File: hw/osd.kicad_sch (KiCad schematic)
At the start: 62 parts, among them U801 SN74CBTLV3125RGYR, U802 XLV320ADC5140IRTWR, U803 SN74CBTLV3125RGYR, U804 SN74CBTLV3125RGYR, U805 SN74CBTLV3125RGYR

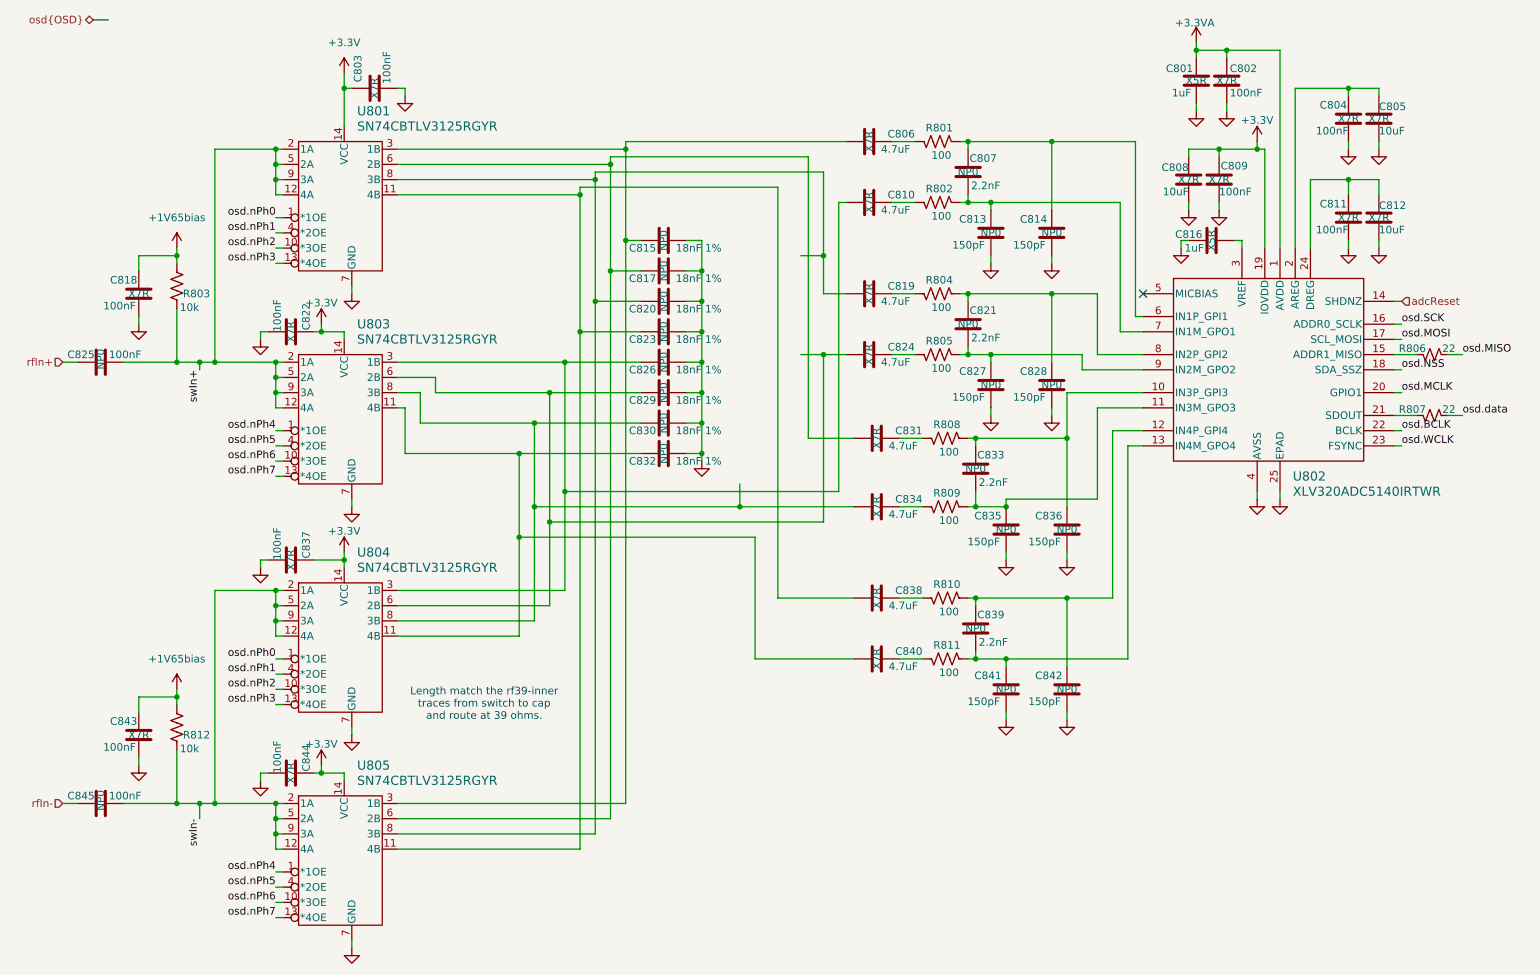
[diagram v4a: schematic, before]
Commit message: Not proud of the rats nest of controls for attenuator and filter, but now I have four filters (not five), all DRC pass, 3D renders properly, and I may tidy it up a bit later.
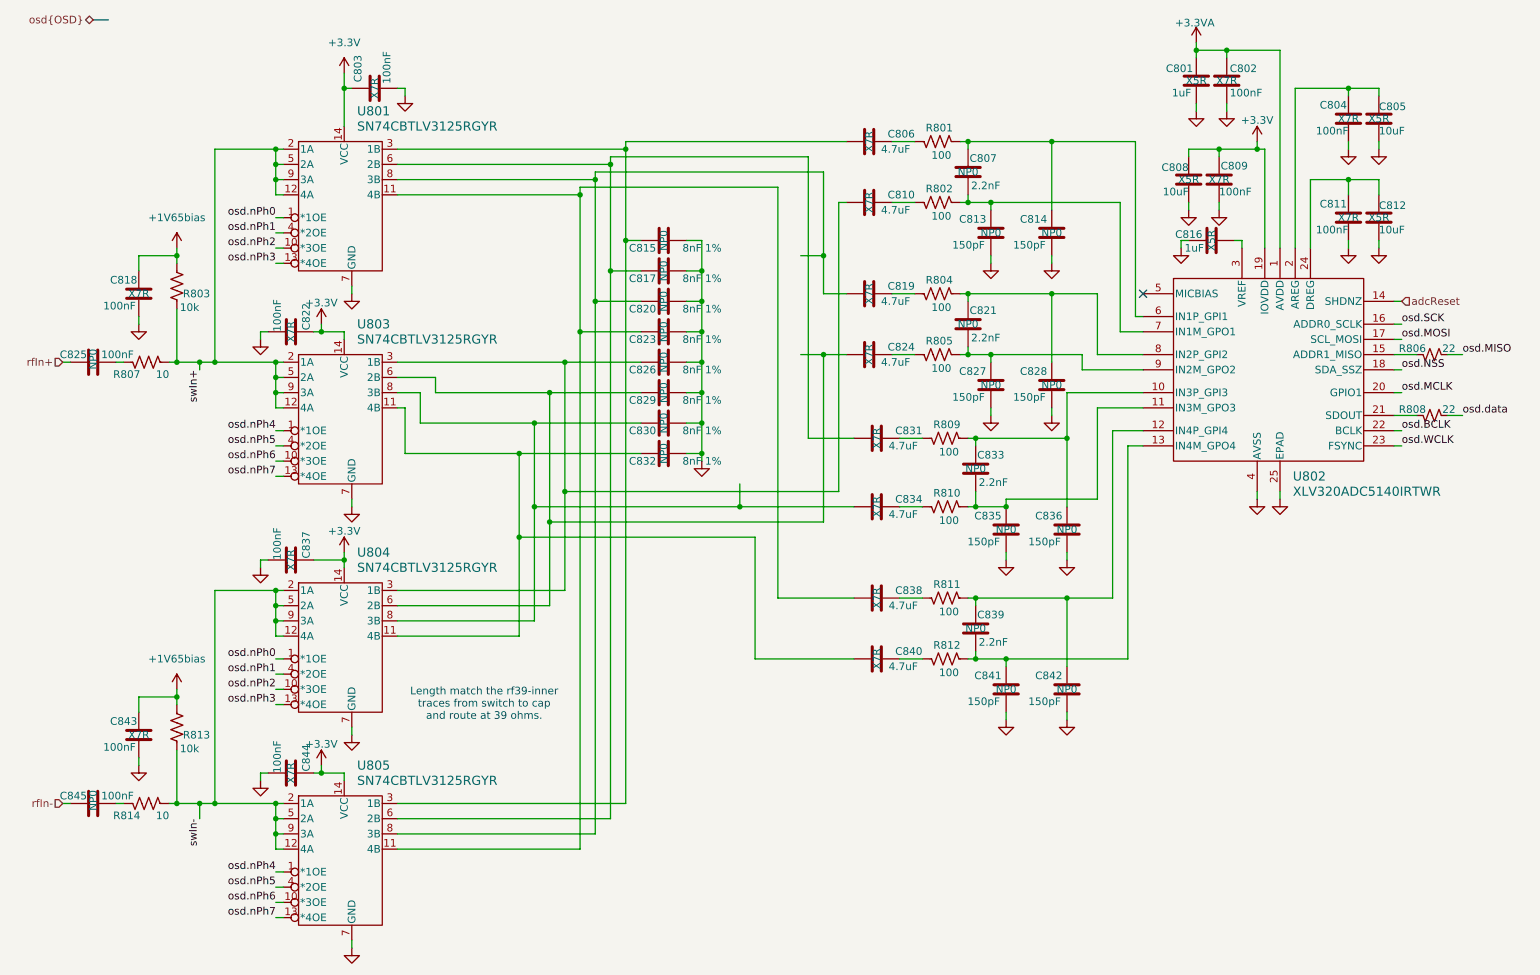
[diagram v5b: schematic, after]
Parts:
- added R807, R814: 10, Resistor_SMD:R_0402_1005Metric, symbol Device:R_US
- C805, C808, C812: footprint Capacitor_SMD:C_0603_1608Metric -> Capacitor_SMD:C_0402_1005Metric; cap-type X7R -> X5R; working-voltage 25V -> 10V
- C807, C821, C833, C839: footprint Capacitor_SMD:C_0603_1608Metric -> Capacitor_SMD:C_0402_1005Metric
- C815, C817, C820, C823, C826, C829, C830, C832: value 18nF 1% -> 8nF 1%
- renumbered R807 to R808, R808 to R809, R809 to R810, R810 to R811, R811 to R812, R812 to R813
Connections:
- net swIn+: now also R807.2; no longer C825.2
- net swIn-: now also R814.2; no longer C845.2
- new net: C845.2, R814.1
- new net: C825.2, R807.1
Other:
- moved on the sheet: C825, C845

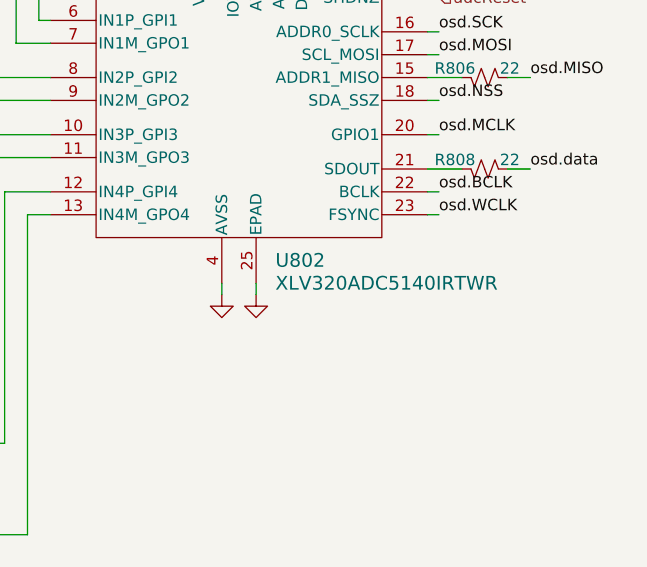
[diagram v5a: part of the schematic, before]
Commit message: Set up for DVT2 PCBA build at JLCPCB
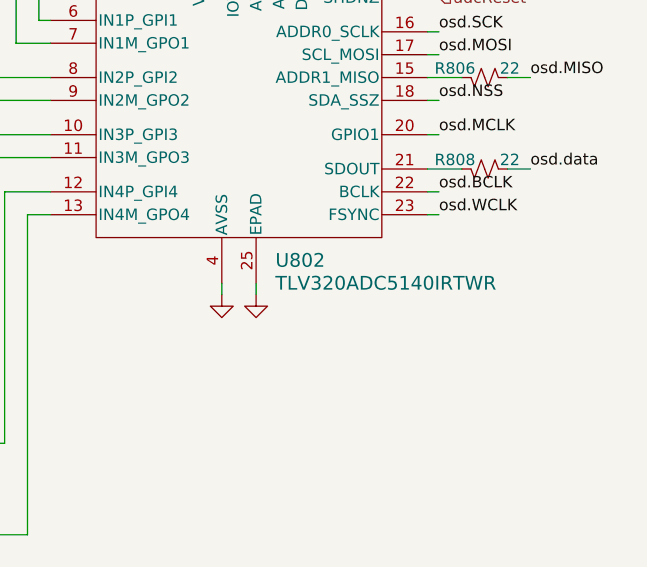
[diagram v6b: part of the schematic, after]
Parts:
- C801, C816: MPN GRM155R61E105KE11D -> (none)
- C802, C803, C804, C809, C811, C818, C822, C837, C843, C844: MPN C0805F104K1RACAUTO -> (none)
- C805, C808, C812: MPN TAJD106K050RNJ -> (none)
- C813, C814, C827, C828, C835, C836, C841, C842: MPN 06033A151FAT2A -> (none)
- C815, C817, C820, C823, C826, C829, C830, C832: JLCPCBpn C106211 -> (none)
- C825, C845: Mouser Part Number (none) -> 81-GRM3195C2A104JA1D
- U802: value XLV320ADC5140IRTWR -> TLV320ADC5140IRTWR; MFG (none) -> TI; MPN (none) -> TLV320ADC5140IRTWR
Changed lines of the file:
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@@
 			)
 		)
+		(property "Mouser Part Number" "81-GRM3195C2A104JA1D"
+			(at 25.4 148.59 90)
+			(effects
+				(font
+					(size 1.27 1.27)
+				)
+				(hide yes)
+			)
+		)
 		(pin "2"
 		)
@@
 			)
 		)
-		(property "MPN" "TAJD106K050RNJ"
+		(property "MPN" ""
 			(at 486.41 -107.95 0)
 			(effects
@@
 			)
 		)
-		(property "JLCPCBpn" "C106211"
+		(property "JLCPCBpn" ""
 			(at 120.65 64.77 0)
 			(effects
@@
 			)
 		)
-		(property "MPN" "C0805F104K1RACAUTO"
+		(property "MPN" ""
 			(at 414.02 -109.22 0)
 			(effects
@@
 			)
 		)
-		(property "Value" "XLV320ADC5140IRTWR"
+		(property "Value" "TLV320ADC5140IRTWR"
 			(at 225.6633 96.52 0)
 			(effects
@@
 			)
 		)
-		(property "Datasheet" "XLV320ADC5140IRTWR"
+		(property "Datasheet" "https://www.ti.com/lit/gpn/tlv320adc5140"
 			(at 142.24 132.08 0)
 			(effects
@@
 			)
 		)
+		(property "cap-type" ""
+			(at 220.98 74.93 0)
+			(effects
+				(font
+					(size 1.27 1.27)
+				)
+			)
+		)
+		(property "r-power" ""
+			(at 220.98 74.93 0)
+			(effects
+				(font
+					(size 1.27 1.27)
+				)
+			)
+		)
+		(property "label" ""
+			(at 220.98 74.93 0)
+			(effects
+				(font
+					(size 1.27 1.27)
+				)
+			)
+		)
+		(property "MPN" "TLV320ADC5140IRTWR"
+			(at 220.98 74.93 0)
+			(effects
+				(font
+					(size 1.27 1.27)
+				)
+				(hide yes)
+			)
+		)
+		(property "MFG" "TI"
+			(at 220.98 74.93 0)
+			(effects
+				(font
+					(size 1.27 1.27)
+				)
+				(hide yes)
+			)
+		)
 		(pin "2"
 		)
@@
 			)
 		)
-		(property "JLCPCBpn" "C106211"
+		(property "JLCPCBpn" ""
 			(at 120.65 80.01 0)
 			(effects
@@
 			)
 		)
-		(property "JLCPCBpn" "C106211"
+		(property "JLCPCBpn" ""
 			(at 120.65 74.93 0)
 			(effects
@@
 			)
 		)
-		(property "MPN" "GRM155R61E105KE11D"
+		(property "MPN" ""
 			(at 88.9 -182.88 0)
 			(effects
@@
 			)
 		)
-		(property "MPN" "06033A151FAT2A"
+		(property "MPN" ""
 			(at 17.78 53.34 0)
 			(effects
@@
 			)
 		)
-		(property "MPN" "C0805F104K1RACAUTO"
+		(property "MPN" ""
 			(at 317.5 -20.32 0)
 			(effects
@@
 			)
 		)
-		(property "MPN" "06033A151FAT2A"
+		(property "MPN" ""
 			(at 25.4 2.54 0)
 			(effects
@@
 			)
 		)
-		(property "MPN" "C0805F104K1RACAUTO"
+		(property "MPN" ""
 			(at 130.81 -26.67 0)
 			(effects
@@
 			)
 		)
-		(property "MPN" "06033A151FAT2A"
+		(property "MPN" ""
 			(at 15.24 2.54 0)
 			(effects
@@
 			)
 		)
-		(property "MPN" "TAJD106K050RNJ"
+		(property "MPN" ""
 			(at 486.41 -124.46 0)
 			(effects
@@
 			)
 		)
-		(property "MPN" "C0805F104K1RACAUTO"
+		(property "MPN" ""
 			(at 181.61 314.96 0)
 			(effects
@@
 			)
 		)
-		(property "JLCPCBpn" "C106211"
+		(property "JLCPCBpn" ""
 			(at 120.65 69.85 0)
 			(effects
@@
 			)
 		)
-		(property "MPN" "06033A151FAT2A"
+		(property "MPN" ""
 			(at 27.94 53.34 0)
 			(effects
@@
 			)
 		)
-		(property "MPN" "06033A151FAT2A"
+		(property "MPN" ""
 			(at 17.78 26.67 0)
 			(effects
@@
 			)
 		)
-		(property "JLCPCBpn" "C106211"
+		(property "JLCPCBpn" ""
 			(at 120.65 54.61 0)
 			(effects
@@
 			)
 		)
-		(property "MPN" "TAJD106K050RNJ"
+		(property "MPN" ""
 			(at -38.1 -114.3 0)
 			(effects
@@
 			)
 		)
-		(property "MPN" "06033A151FAT2A"
+		(property "MPN" ""
 			(at 27.94 26.67 0)
 			(effects
@@
 			)
 		)
-		(property "JLCPCBpn" "C106211"
+		(property "JLCPCBpn" ""
 			(at 120.65 59.69 0)
 			(effects
@@
 			)
 		)
-		(property "MPN" "C0805F104K1RACAUTO"
+		(property "MPN" ""
 			(at 115.57 66.04 0)
 			(effects
@@
 			)
 		)
-		(property "MPN" "C0805F104K1RACAUTO"
+		(property "MPN" ""
 			(at 317.5 -36.83 0)
 			(effects
@@
 			)
 		)
-		(property "MPN" "C0805F104K1RACAUTO"
+		(property "MPN" ""
 			(at 181.61 353.06 0)
 			(effects
@@
 			)
 		)
-		(property "MPN" "C0805F104K1RACAUTO"
+		(property "MPN" ""
 			(at -50.8 274.32 0)
 			(effects
@@
 			)
 		)
-		(property "JLCPCBpn" "C106211"
+		(property "JLCPCBpn" ""
 			(at 120.65 90.17 0)
 			(effects
@@
 			)
 		)
-		(property "MPN" "06033A151FAT2A"
+		(property "MPN" ""
 			(at 25.4 -22.86 0)
 			(effects
@@
 			)
 		)
+		(property "Mouser Part Number" "81-GRM3195C2A104JA1D"
+			(at 25.4 74.93 90)
+			(effects
+				(font
+					(size 1.27 1.27)
+				)
+				(hide yes)
+			)
+		)
 		(pin "2"
 		)
@@
 			)
 		)
-		(property "MPN" "06033A151FAT2A"
+		(property "MPN" ""
 			(at 15.24 -22.86 0)
 			(effects
@@
 			)
 		)
-		(property "JLCPCBpn" "C106211"
+		(property "JLCPCBpn" ""
 			(at 120.65 85.09 0)
 			(effects
@@
 			)
 		)
-		(property "MPN" "C0805F104K1RACAUTO"
+		(property "MPN" ""
 			(at 115.57 -7.62 0)
 			(effects
@@
 			)
 		)
-		(property "MPN" "C0805F104K1RACAUTO"
+		(property "MPN" ""
 			(at 181.61 388.62 0)
 			(effects
@@
 			)
 		)
-		(property "MPN" "GRM155R61E105KE11D"
+		(property "MPN" ""
 			(at 447.04 151.13 0)
 			(effects

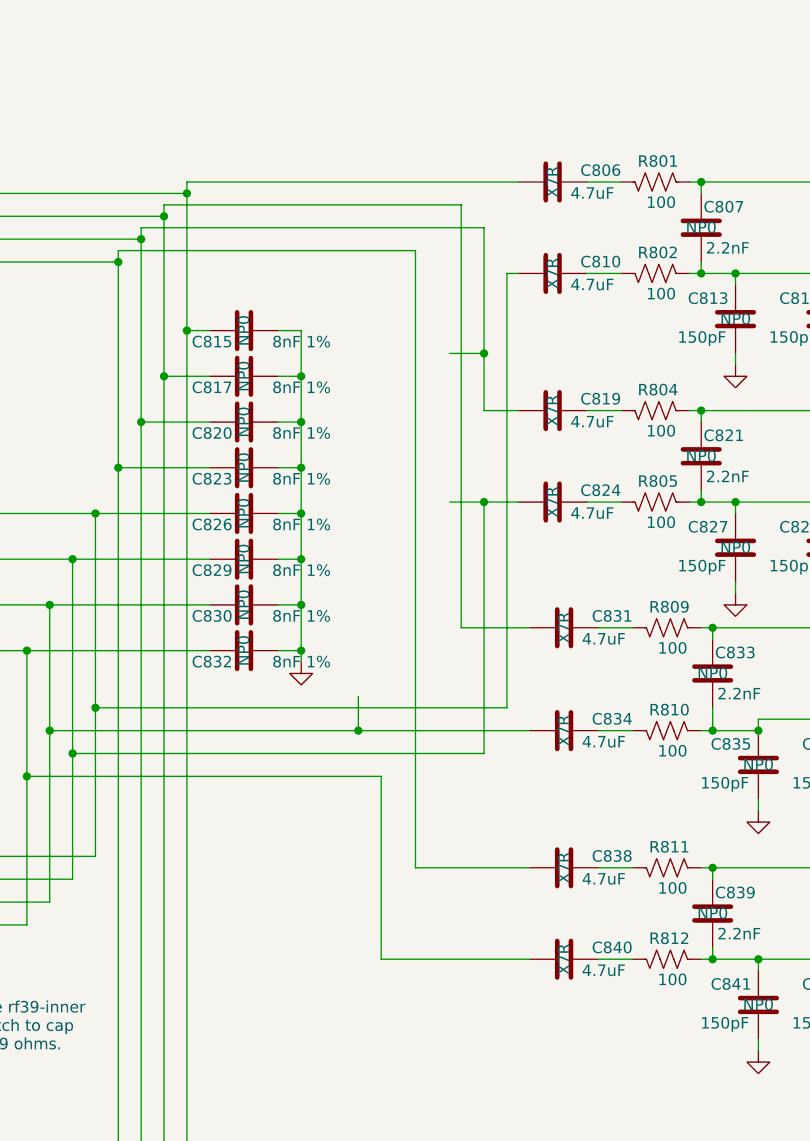
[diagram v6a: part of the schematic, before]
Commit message: Switch to parts I can source from Mouser
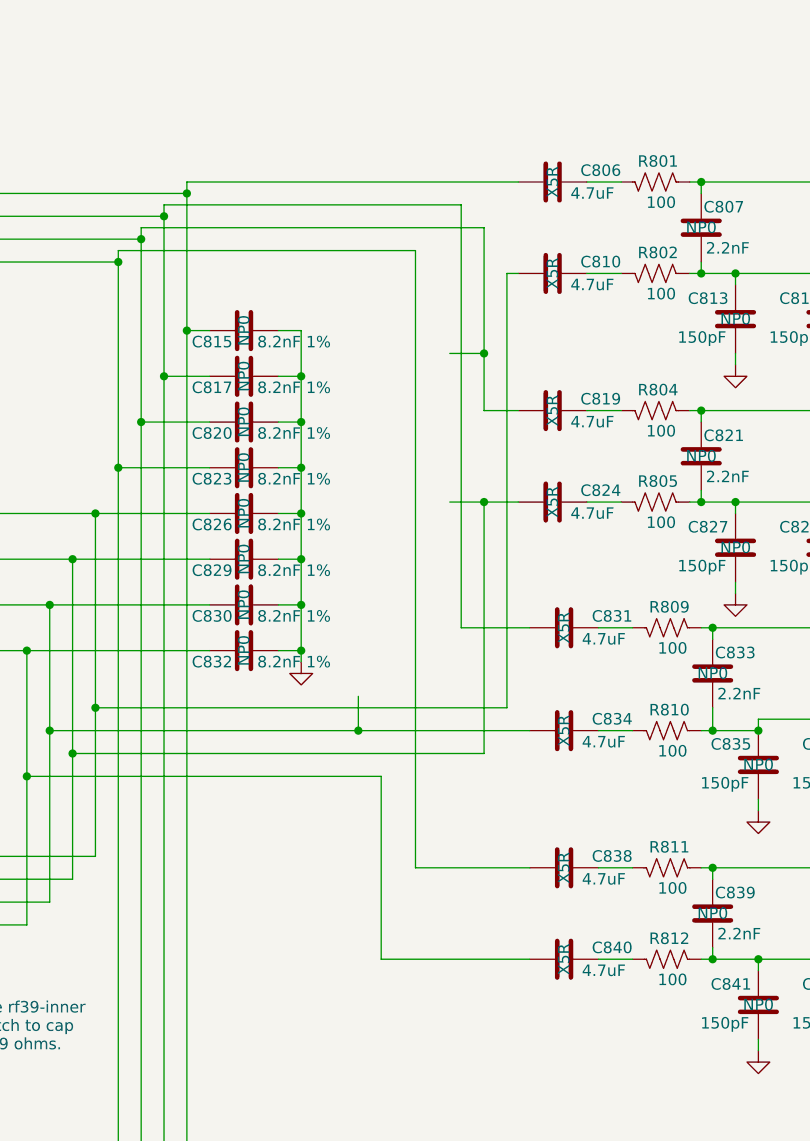
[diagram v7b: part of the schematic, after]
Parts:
- C801, C816: MFG (none) -> muRata; MPN (none) -> GRM155R61E105MA12D; Mouser Part Number (none) -> 81-GRM155R61E105MA2D
- C802, C803, C804, C809, C811, C818, C822, C837, C843, C844: MFG (none) -> muRata; MPN (none) -> GCM155R71H104KE02D; Mouser Part Number (none) -> 81-GCM155R71H104KE2D
- C805, C808, C812: MFG (none) -> Samsung; MPN (none) -> CL05A106MP6NUN8; Mouser Part Number (none) -> 187-CL05A106MP6NUN8
- C806, C810, C819, C824, C831, C834, C838, C840: MFG (none) -> Kyocera; MPN (none) -> CM05X5R475M10AH; Mouser Part Number (none) -> 346-CM05X5R475M10AH; cap-type X7R -> X5R; working-voltage 25V -> 10V
- C807, C821, C833, C839: MFG (none) -> KEMET; MPN (none) -> C0402C222K3GECTU; Mouser Part Number (none) -> 80-C0402C222K3GECTU
- C813, C814, C827, C828, C835, C836, C841, C842: MFG (none) -> Kyocera; MPN (none) -> 04023A151JAT2A; Mouser Part Number (none) -> 581-04023A151J
- C815, C817, C820, C823, C826, C829, C830, C832: value 8nF 1% -> 8.2nF 1%; MFG (none) -> Kyocera; MPN (none) -> 08053A822FAT2A; Mouser Part Number (none) -> 581-08053A822FAT2A
- C825, C845: MFG (none) -> muRata

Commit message: Updates for actual DVT2 BOM order part numbers and fixes
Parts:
- C813, C814, C827, C828, C835, C836, C841, C842: MFG Kyocera -> KEMET; MPN 04023A151JAT2A -> C0402C151J3GACTU; Mouser Part Number 581-04023A151J -> C0402C151J3GACTU
- R801, R802, R804, R805, R809, R810, R811, R812: MFG (none) -> Vishay; MPN (none) -> MCS04020C1000FE000; Mouser Part Number (none) -> 594-MCS04020C1000FE0
- R803, R813: MFG (none) -> YAGEO; MPN (none) -> RT0402BRD0710KL; Mouser Part Number (none) -> 603-RT0402BRD0710KL
- R806, R808: MFG (none) -> Wurth Electronik; MPN (none) -> 560112110216; Mouser Part Number (none) -> 710-560112110216
- R807, R814: MFG (none) -> YAGEO; MPN (none) -> RE0402FRE0710RL; Mouser Part Number (none) -> 603-RE0402FRE0710RL
- U801, U803, U804, U805: MFG (none) -> TI; MPN (none) -> SN74CBTLV3125RGYR; Mouser Part Number (none) -> 595-SN74CBTLV3125RGYR
- U802: Mouser Part Number (none) -> 595-V320ADC5140IRTWR
